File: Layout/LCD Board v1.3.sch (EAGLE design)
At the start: 37 parts, among them IC1 MAX3232CPE, IC2 MAX3232CPE, IC3 788TV, IC4 788TV

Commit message: Spannungsregler zu lm1117 und Input Cap hinzugefügt
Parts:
- added C13, C14: 10uF, rcl:CPOL-EUE2-4
- C11, C5: value 500uF -> 10uF
- renumbered IC3 to LM1117, IC4 to LM117
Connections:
- net +12V: now also C13.+, C14.+
- net GND: now also C13.-, C14.-
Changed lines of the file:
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@@
 <part name="X1" library="con-subd" deviceset="F09" device="H"/>
 <part name="GND5" library="supply2" deviceset="GND" device=""/>
-<part name="IC3" library="linear" deviceset="78*" device="TV" technology="8"/>
+<part name="LM1117" library="linear" deviceset="78*" device="TV" technology="8"/>
 <part name="GND6" library="supply2" deviceset="GND" device=""/>
 <part name="VCC4" library="supply1" deviceset="VCC" device=""/>
@@
 <part name="GND8" library="supply2" deviceset="GND" device=""/>
 <part name="VCC7" library="supply1" deviceset="VCC" device=""/>
-<part name="C5" library="rcl" deviceset="CPOL-EU" device="E2-4" value="500uF"/>
+<part name="C5" library="rcl" deviceset="CPOL-EU" device="E2-4" value="10uF"/>
 <part name="C6" library="rcl" deviceset="C-EU" device="025-030X050"/>
 <part name="P+2" library="supply1" deviceset="+12V" device=""/>
@@
 <part name="X2" library="con-subd" deviceset="F09" device="H"/>
 <part name="GND14" library="supply2" deviceset="GND" device=""/>
-<part name="IC4" library="linear" deviceset="78*" device="TV" technology="8"/>
+<part name="LM117" library="linear" deviceset="78*" device="TV" technology="8"/>
 <part name="GND15" library="supply2" deviceset="GND" device=""/>
 <part name="VCC12" library="supply1" deviceset="VCC" device=""/>
 <part name="P+3" library="supply1" deviceset="+12V" device=""/>
-<part name="C11" library="rcl" deviceset="CPOL-EU" device="E2-4" value="500uF"/>
+<part name="C11" library="rcl" deviceset="CPOL-EU" device="E2-4" value="10uF"/>
 <part name="P+5" library="supply1" deviceset="+12V" device=""/>
 <part name="GND17" library="supply2" deviceset="GND" device=""/>
@@
 <part name="JP2" library="pinhead" deviceset="PINHD-1X3" device=""/>
 <part name="JP3" library="pinhead" deviceset="PINHD-1X2" device=""/>
+<part name="C13" library="rcl" deviceset="CPOL-EU" device="E2-4" value="10uF"/>
+<part name="C14" library="rcl" deviceset="CPOL-EU" device="E2-4" value="10uF"/>
 </parts>
 <sheets>
@@
 <attribute name="VALUE" x="235.585" y="-38.735" size="1.778" layer="96" rot="R270"/>
 </instance>
-<instance part="IC3" gate="A1" x="73.66" y="68.58"/>
+<instance part="LM1117" gate="A1" x="73.66" y="68.58"/>
 <instance part="GND6" gate="GND" x="73.66" y="53.34" smashed="yes">
 <attribute name="VALUE" x="71.755" y="50.165" size="1.778" layer="96"/>
@@
 <instance part="R2" gate="G$1" x="-20.32" y="0"/>
 <instance part="JP1" gate="A" x="134.62" y="10.16"/>
+<instance part="C13" gate="G$1" x="60.96" y="58.42" rot="MR270"/>
 </instances>
 <busses>
@@
 </segment>
 <segment>
-<pinref part="IC3" gate="A1" pin="GND"/>
+<pinref part="LM1117" gate="A1" pin="GND"/>
 <pinref part="GND6" gate="GND" pin="GND"/>
 <wire x1="73.66" y1="55.88" x2="73.66" y2="58.42" width="0.1524" layer="91"/>
@@
 <wire x1="81.28" y1="58.42" x2="73.66" y2="58.42" width="0.1524" layer="91"/>
 <junction x="73.66" y="58.42"/>
+<pinref part="C13" gate="G$1" pin="-"/>
+<wire x1="66.04" y1="58.42" x2="73.66" y2="58.42" width="0.1524" layer="91"/>
 </segment>
 <segment>
@@
 </segment>
 <segment>
-<pinref part="IC3" gate="A1" pin="VO"/>
+<pinref part="LM1117" gate="A1" pin="VO"/>
 <pinref part="VCC4" gate="VCC" pin="VCC"/>
 <wire x1="99.06" y1="68.58" x2="91.44" y2="68.58" width="0.1524" layer="91"/>
@@
 <net name="+12V" class="0">
 <segment>
-<pinref part="IC3" gate="A1" pin="VI"/>
+<pinref part="LM1117" gate="A1" pin="VI"/>
 <pinref part="P+1" gate="1" pin="+12V"/>
-<wire x1="53.34" y1="68.58" x2="63.5" y2="68.58" width="0.1524" layer="91"/>
+<wire x1="53.34" y1="68.58" x2="58.42" y2="68.58" width="0.1524" layer="91"/>
+<pinref part="C13" gate="G$1" pin="+"/>
+<wire x1="58.42" y1="68.58" x2="63.5" y2="68.58" width="0.1524" layer="91"/>
+<wire x1="58.42" y1="58.42" x2="58.42" y2="68.58" width="0.1524" layer="91"/>
+<junction x="58.42" y="68.58"/>
 </segment>
 <segment>
@@
 <attribute name="VALUE" x="222.885" y="14.605" size="1.778" layer="96" rot="R270"/>
 </instance>
-<instance part="IC4" gate="A1" x="73.66" y="68.58"/>
+<instance part="LM117" gate="A1" x="73.66" y="68.58"/>
 <instance part="GND15" gate="GND" x="73.66" y="53.34" smashed="yes">
 <attribute name="VALUE" x="71.755" y="50.165" size="1.778" layer="96"/>
@@
 <instance part="JP2" gate="A" x="157.48" y="50.8"/>
 <instance part="JP3" gate="G$1" x="81.28" y="38.1"/>
+<instance part="C14" gate="G$1" x="60.96" y="58.42" rot="MR270"/>
 </instances>
 <busses>
@@
 </segment>
 <segment>
-<pinref part="IC4" gate="A1" pin="GND"/>
+<pinref part="LM117" gate="A1" pin="GND"/>
 <pinref part="GND15" gate="GND" pin="GND"/>
 <wire x1="73.66" y1="55.88" x2="73.66" y2="58.42" width="0.1524" layer="91"/>
@@
 <wire x1="81.28" y1="58.42" x2="73.66" y2="58.42" width="0.1524" layer="91"/>
 <junction x="73.66" y="58.42"/>
+<pinref part="C14" gate="G$1" pin="-"/>
+<wire x1="66.04" y1="58.42" x2="73.66" y2="58.42" width="0.1524" layer="91"/>
 </segment>
 <segment>
@@
 </segment>
 <segment>
-<pinref part="IC4" gate="A1" pin="VO"/>
+<pinref part="LM117" gate="A1" pin="VO"/>
 <pinref part="VCC12" gate="VCC" pin="VCC"/>
 <wire x1="99.06" y1="68.58" x2="91.44" y2="68.58" width="0.1524" layer="91"/>
@@
 <net name="+12V" class="0">
 <segment>
-<pinref part="IC4" gate="A1" pin="VI"/>
+<pinref part="LM117" gate="A1" pin="VI"/>
 <pinref part="P+3" gate="1" pin="+12V"/>
-<wire x1="53.34" y1="68.58" x2="63.5" y2="68.58" width="0.1524" layer="91"/>
-</segment>
-<segment>
+<wire x1="53.34" y1="68.58" x2="58.42" y2="68.58" width="0.1524" layer="91"/>
+<pinref part="C14" gate="G$1" pin="+"/>
+<wire x1="58.42" y1="68.58" x2="63.5" y2="68.58" width="0.1524" layer="91"/>
+<wire x1="58.42" y1="58.42" x2="58.42" y2="68.58" width="0.1524" layer="91"/>
+<junction x="58.42" y="68.58"/>
+</segment>
+<segment>

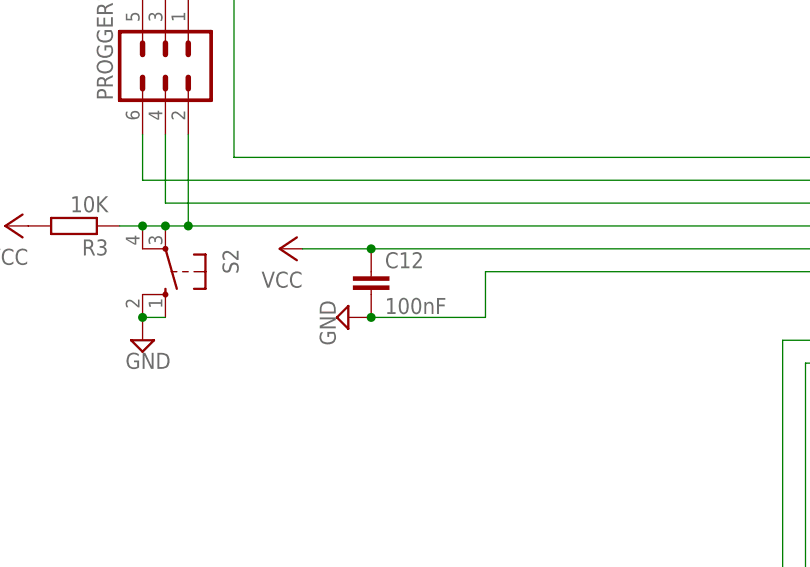
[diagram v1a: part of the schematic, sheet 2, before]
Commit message: Kleinere  Layoutchanges und Layouts zum Ausdrucken
Messplatine hinzugefüg
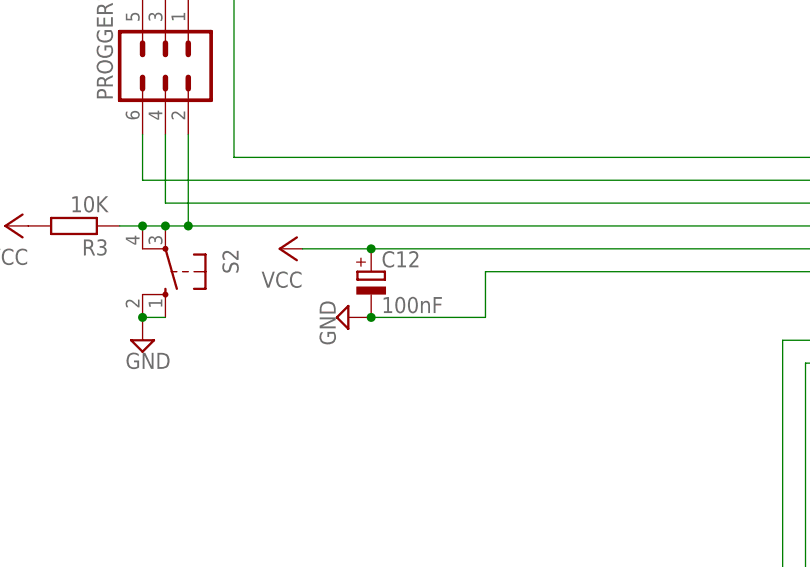
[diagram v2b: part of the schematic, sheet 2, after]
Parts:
- C10, C11, C13, C14, C2, C4, C8: device rcl:CPOL-EUE2-4 -> rcl:CPOL-EUE2.5-4V
- C12: device rcl:C-EU025-030X050 -> rcl:CPOL-EUE2.5-4V
- C5: device rcl:CPOL-EUE2-4 -> rcl:CPOL-EUE3.5-8
- R1, R9: device resistor:R-EU_0204/5 -> rcl:R-EU_0204/7
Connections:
- removed net GND: C10.+, C11.-, C12.2, C13.-, C14.-, C4.+, C5.-, C6.2, IC5.11, IC5.31, IC6.11, IC6.31, IC7.4, JP1.7, JP2.2, JP3.2, LM1117.GND, LM117.GND, PROGGER.1, PROGGER1.1, R4.2, R8.A, R9.2, S1.S, S1.S1, S2.S, S2.S1, X1.1, X2.1, X2.7
- new net $N4: C10.+, C11.-, C12.-, C13.-, C14.-, C4.+, C5.-, C6.2, IC5.11, IC5.31, IC6.11, IC6.31, IC7.4, JP1.7, JP2.2, JP3.2, LM1117.GND, LM117.GND, PROGGER.1, PROGGER1.1, R4.2, R8.A, R9.2, S1.S, S1.S1, S2.S, S2.S1, X1.1, X2.1, X2.7
- net VCC: now also C12.+; no longer C12.1
